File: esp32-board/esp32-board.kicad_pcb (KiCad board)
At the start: 2 copper layers, 116.2 x 30 mm, 32 parts, among them J1 remote_header, J3 SOIL_SENSOR, J4 ANT, J5 Conn_01x10_Pin, J6 Conn_01x10_Pin, J7 Battery, SW1 RESET, SW2 ESP Program, SW3 RESET, U1 ESP32-WROOM-32D, U2 XC6220B331MR, U3 XC6220B331MR, U4 TPS3839DBZ, U5 RFM95W-915S2, U6 MAX17048G_T10

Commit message: ADD: Final PCB
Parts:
- added G***: LOGO, LOGO:logo, F.Cu at (152.2, 63.9)
- added G***: LOGO, LOGO:logo, B.Cu at (152.6, 64.1)
- + BAT -: renamed from J7
- C1, C9: footprint Capacitor_SMD:C_1812_4532Metric_Pad1.57x3.40mm_HandSolder -> Capacitor_SMD:C_1206_3216Metric_Pad1.33x1.80mm_HandSolder
- CONFIG RESET: renamed from SW3; value RESET -> WEB_CONF
- EXTERNAL CONTROL: renamed from J1
- SOIL SENSOR: renamed from J3
- moved C2 176.2 mm to (80.9, 98.5), turned to 180 degrees
- moved C4 152.9 mm to (103.9, 68.2), turned to 180 degrees
- moved C5 152.3 mm to (104.0, 78.7), turned to 180 degrees
- moved C10 148.9 mm to (110.4, 69.1)
- moved C3 146.7 mm to (81.1, 93.8), turned to 180 degrees
- moved C6 146.7 mm to (110.1, 75.5), turned to -90 degrees
- moved C11 144.1 mm to (116.0, 69.1)
- moved R1 131.8 mm to (103.9, 93.9), turned to 90 degrees
- moved C7 129.9 mm to (127.4, 75.4), turned to 90 degrees
- moved R3 125.1 mm to (122.1, 70.1), turned to -90 degrees
- moved R4 123.8 mm to (122.4, 75.5), turned to 90 degrees
- moved R5 123.2 mm to (129.0, 68.5), turned to 90 degrees
- moved R6 119.5 mm to (132.7, 73.0), turned to 90 degrees
- moved C8 105.3 mm to (151.2, 87.3), turned to 90 degrees
- moved R2 104.0 mm to (143.7, 71.5)
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- renumbered J4 to ANT, SW2 to PROG, SW1 to RESET
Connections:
- EXTERNAL CONTROL pad 4: ESP_TX -> ESP_RX
- EXTERNAL CONTROL pad 5: ESP_RX -> ESP_TX
- J5 pad 1: ESP_PROG -> GPIO23
- J5 pad 10: GPIO_15 -> GPIO02
- J5 pad 2: ESP_ENA -> I2C_SCL
- J5 pad 3: GND -> ESP_TX
- J5 pad 4: VCC -> ESP_RX
- J5 pad 5: VCC_AUX -> I2C_SDA
- J5 pad 6: START_WEB_CONFIG -> LED_DATA_PIN
- J5 pad 7: GPIO02 -> START_WEB_CONFIG
- J5 pad 9: GPIO_12 -> ESP_PROG
- J6 pad 1: GPIO_17 -> GND
- J6 pad 10: ESP_RX -> ESP_ENA
- J6 pad 2: I2C_SDA -> VCC
- J6 pad 3: I2C_SCL -> VCC_AUX
- J6 pad 4: GPIO23 -> SENSOR_VP
- J6 pad 5: BAT_ALERT -> SENSOR_VN
- J6 pad 7: SENSOR_VN -> BAT_ALERT
- J6 pad 8: SENSOR_VP -> GPIO_12
- J6 pad 9: ESP_TX -> GPIO_15
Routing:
- net ESP_ENA: track 0.00 -> 136.0 mm, vias 0 -> 2
- net ESP_PROG: track 0.00 -> 105.6 mm, vias 0 -> 2
- net START_WEB_CONFIG: track 0.00 -> 88.6 mm, vias 0 -> 2
- net VCC: track 0.00 -> 86.1 mm, vias 0 -> 3
- net LORA_DIO2: track 0.00 -> 74.6 mm, vias 0 -> 2
- net I2C_SCL: track 0.00 -> 71.8 mm, vias 0 -> 3
- net LORA_DIO1: track 0.00 -> 68.1 mm, vias 0 -> 2
- net SOIL_SENSOR: track 0.00 -> 67.8 mm
- net I2C_SDA: track 0.00 -> 65.2 mm, vias 0 -> 3
- net BAT_ALERT: track 0.00 -> 64.2 mm, vias 0 -> 4
- net LORA_DIO0: track 0.00 -> 63.3 mm, vias 0 -> 4
- net ESP_TX: track 0.00 -> 59.4 mm
- net LORA_NSS: track 0.00 -> 57.9 mm, vias 0 -> 2
- net LORA_SCK: track 0.00 -> 57.2 mm, vias 0 -> 2
- net ESP_RX: track 0.00 -> 56.5 mm
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- added copper zone on B.Cu, net GND
- added copper zone on F.Cu, net GND
- added copper zone on In1.Cu, net GND
- added copper zone on In2.Cu, net VCC_AUX
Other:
- board size 116.2 x 30 mm -> 78.7 x 47.4 mm
- copper layers 2 -> 4
- board text added: "+ BAT -"
- board text added: "+ S -"
- board text added: "BAT_ALERT"
- board text added: "GND"
- board text added: "GPIO02"
- board text added: "GPIO04"
- board text added: "GPIO15"
- board text added: "GPIO22"
- board text added: "GPIO23"
- board text added: "GPIO35"
- board text added: "LED_DATA"
- board text added: "PROG"
- board text added: "RESET"
- board text added: "RX"
- board text added: "SCL"
- board text added: "SDA"
- board text added: "SENSOR_VN"
- board text added: "SENSOR_VP"
- board text added: "TX"
- board text added: "VA7RCV"
- board text added: "VCC"
- board text added: "VCC_AUX"
- board text added: "WEB_CONFIG"
- board text added: "https://www.va7rcv.ca"

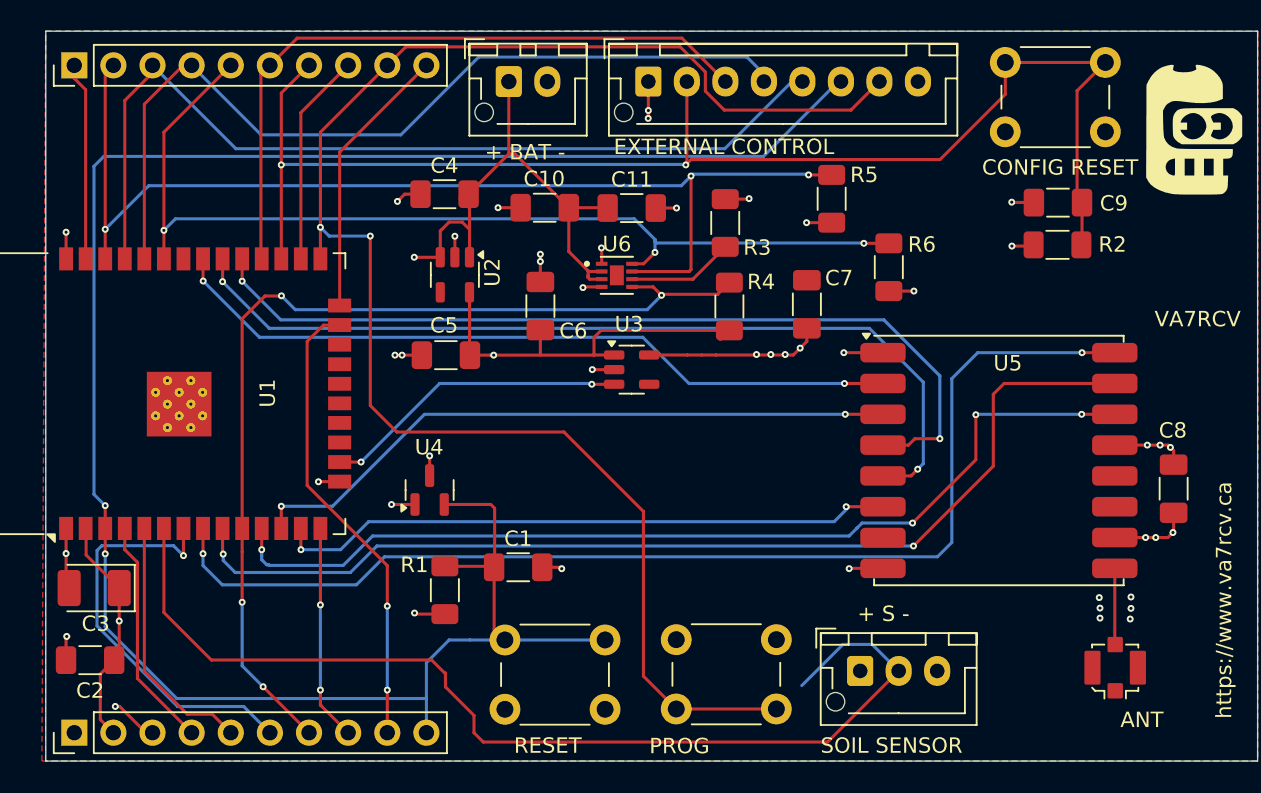
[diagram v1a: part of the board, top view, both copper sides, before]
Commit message: fixes to schematic and PCB
This change contains the following fixes on schematic:
 - U3 VIN is now connected to V_BAT
 - C7 and C5 are now 4.7 uF as specified in data sheet

Changes to PCB:
- Fixed U3 VIN routing
- Simplified routing for PROGRAM and START_WEB_CONFIG switches
- VBAT traces are now 15 mil
- Rerouted traces as to avoid being direclty below ESP and lora modules
- Added dedicated labels to the above switches
- Moved C6 and C7 closer to U3
- Simplified routing of several traces
- Fixed issues with silkscreen

Signed-off-by: Oscar Arias <amanuense@gmail.com>
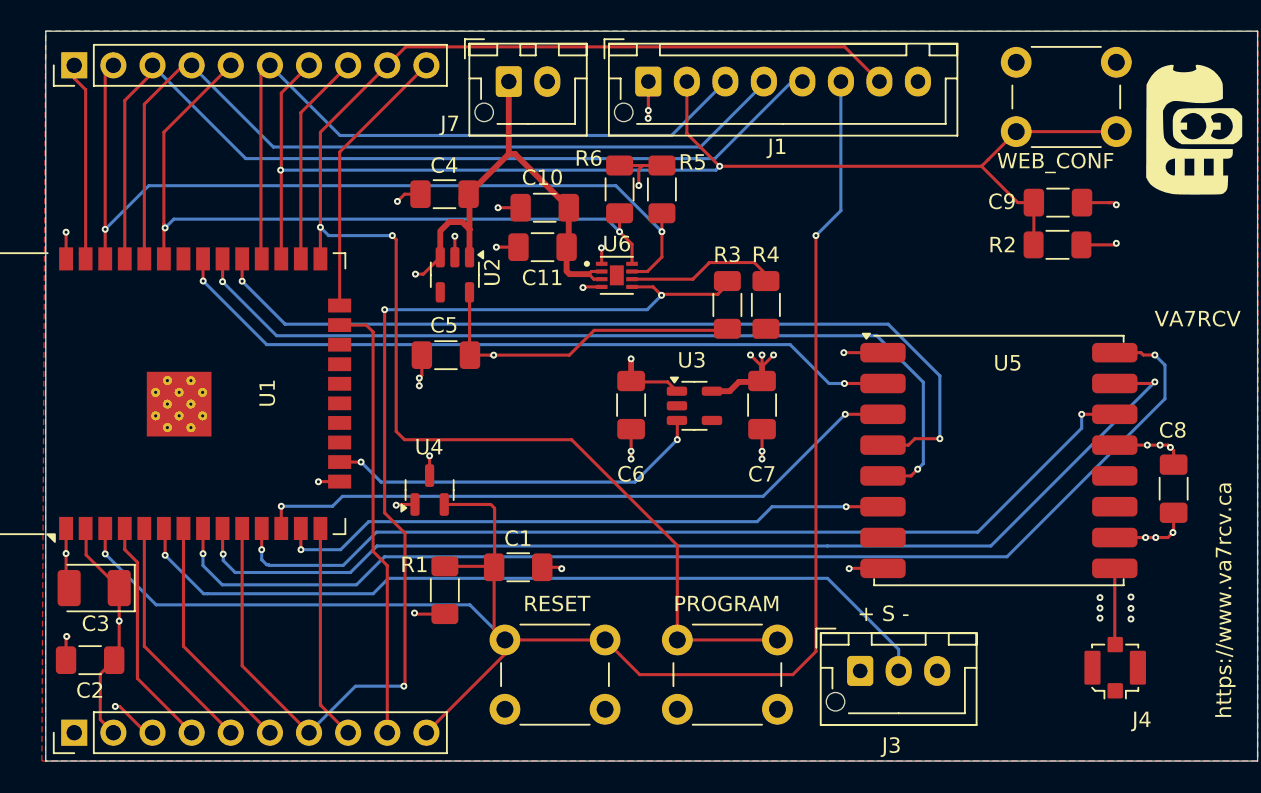
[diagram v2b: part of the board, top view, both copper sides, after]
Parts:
- C5, C7: value 10uF -> 4.7uF
- J1: renamed from EXTERNAL CONTROL
- J3: renamed from SOIL SENSOR
- J7: renamed from + BAT -
- SW3: renamed from CONFIG RESET
- moved R6 18.2 mm to (115.2, 67.9), turned to -90 degrees
- moved R5 11.0 mm to (118.0, 67.9), turned to -90 degrees
- moved C6 8.72 mm to (116.0, 81.9), turned to 90 degrees
- moved SW2 7.97 mm to (125.5, 101.7), turned to 180 degrees
- moved SW3 7.34 mm to (141.0, 59.6), turned to 0 degrees
- moved C7 7.16 mm to (124.5, 81.9), turned to -90 degrees
- moved C11 6.32 mm to (110.2, 71.7), turned to 180 degrees
- moved R3 5.94 mm to (124.8, 75.4), turned to 90 degrees
- moved U3 4.70 mm to (120.1, 82.0)
- moved R4 0.16 mm to (122.2, 75.4)
- turned C9 to 0 degrees
- turned R2 to 180 degrees
- renumbered ANT to J4, RESET to RESET1, PROG to SW2
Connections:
- C6 pad 2: VCC -> V_BAT
- U3 pad 1: VCC -> V_BAT
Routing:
- net ESP_ENA: track 136.0 -> 113.1 mm
- net V_BAT: track 49.3 -> 70.9 mm, vias 2 -> 3
- net I2C_SDA: track 65.2 -> 48.5 mm, vias 3 -> 2
- net I2C_SCL: track 71.8 -> 56.9 mm, vias 3 -> 2
- net SOIL_SENSOR: track 67.8 -> 54.1 mm, vias 0 -> 1
- net GPIO35: track 26.8 -> 15.6 mm, vias 1 -> 0
- net VCC: track 86.1 -> 76.9 mm
- net BAT_ALERT: track 64.2 -> 72.7 mm, vias 4 -> 3
- net START_WEB_CONFIG: track 88.6 -> 82.1 mm
- net ESP_PROG: track 105.6 -> 99.7 mm
- net VCC_AUX_ENA: track 20.1 -> 24.9 mm
- net Net-(U6-QSTRT): track 6.92 -> 9.90 mm
- net LORA_DIO1: track 68.1 -> 70.7 mm
- net VCC_AUX: track 26.5 -> 24.2 mm, vias 13 -> 11
- net LORA_DIO2: track 74.6 -> 76.2 mm
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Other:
- board text added: "PROGRAM"
- board text added: "WEB_CONF"

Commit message: Revert "fixes to schematic and PCB"
This reverts commit 3e7eab6521abb5c68805baea498affc1a11a7eaf.
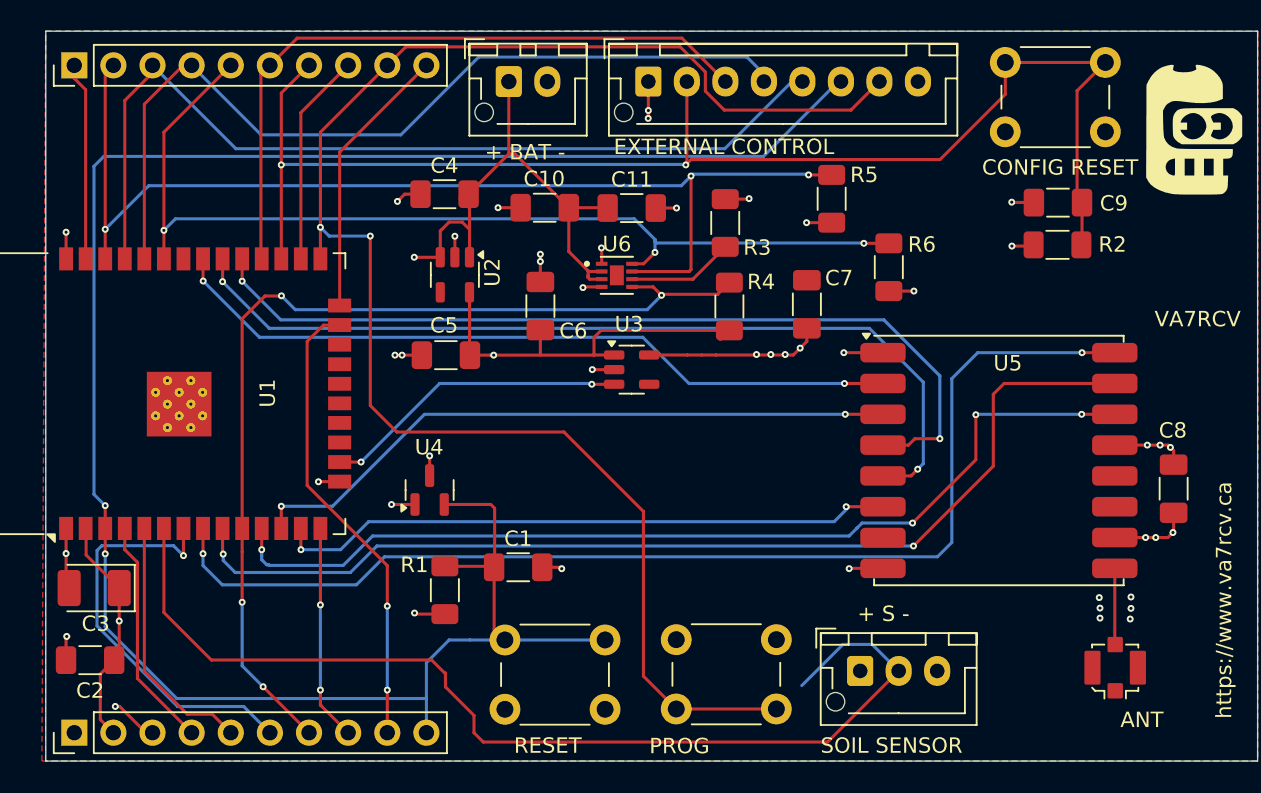
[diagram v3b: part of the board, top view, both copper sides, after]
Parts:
- + BAT -: renamed from J7
- C5, C7: value 4.7uF -> 10uF
- CONFIG RESET: renamed from SW3
- EXTERNAL CONTROL: renamed from J1
- SOIL SENSOR: renamed from J3
- moved R6 18.2 mm to (132.7, 73.0), turned to 90 degrees
- moved R5 11.0 mm to (129.0, 68.5), turned to 90 degrees
- moved C6 8.72 mm to (110.1, 75.5), turned to -90 degrees
- moved PROG 7.97 mm to (118.9, 97.1), turned to 0 degrees
- moved CONFIG RESET 7.34 mm to (146.8, 64.2), turned to 180 degrees
- moved C7 7.16 mm to (127.4, 75.4), turned to 90 degrees
- moved C11 6.32 mm to (116.0, 69.1), turned to 0 degrees
- moved R3 5.94 mm to (122.1, 70.1), turned to -90 degrees
- moved U3 4.70 mm to (116.0, 79.6)
- moved R4 0.16 mm to (122.4, 75.5)
- turned C9 to 180 degrees
- turned R2 to 0 degrees
- renumbered J4 to ANT, SW2 to PROG, RESET1 to RESET
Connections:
- C6 pad 2: V_BAT -> VCC
- U3 pad 1: V_BAT -> VCC
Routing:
- net ESP_ENA: track 113.1 -> 136.0 mm
- net V_BAT: track 70.9 -> 49.3 mm, vias 3 -> 2
- net I2C_SDA: track 48.5 -> 65.2 mm, vias 2 -> 3
- net I2C_SCL: track 56.9 -> 71.8 mm, vias 2 -> 3
- net SOIL_SENSOR: track 54.1 -> 67.8 mm, vias 1 -> 0
- net GPIO35: track 15.6 -> 26.8 mm, vias 0 -> 1
- net VCC: track 76.9 -> 86.1 mm
- net BAT_ALERT: track 72.7 -> 64.2 mm, vias 3 -> 4
- net START_WEB_CONFIG: track 82.1 -> 88.6 mm
- net ESP_PROG: track 99.7 -> 105.6 mm
- net VCC_AUX_ENA: track 24.9 -> 20.1 mm
- net Net-(U6-QSTRT): track 9.90 -> 6.92 mm
- net LORA_DIO1: track 70.7 -> 68.1 mm
- net VCC_AUX: track 24.2 -> 26.5 mm, vias 11 -> 13
- net LORA_DIO2: track 76.2 -> 74.6 mm
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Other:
- board text removed: "PROGRAM"
- board text removed: "WEB_CONF"
